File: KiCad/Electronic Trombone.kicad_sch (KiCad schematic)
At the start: 13 parts, among them J1 691137710004, U1 TL074, U3 TL074

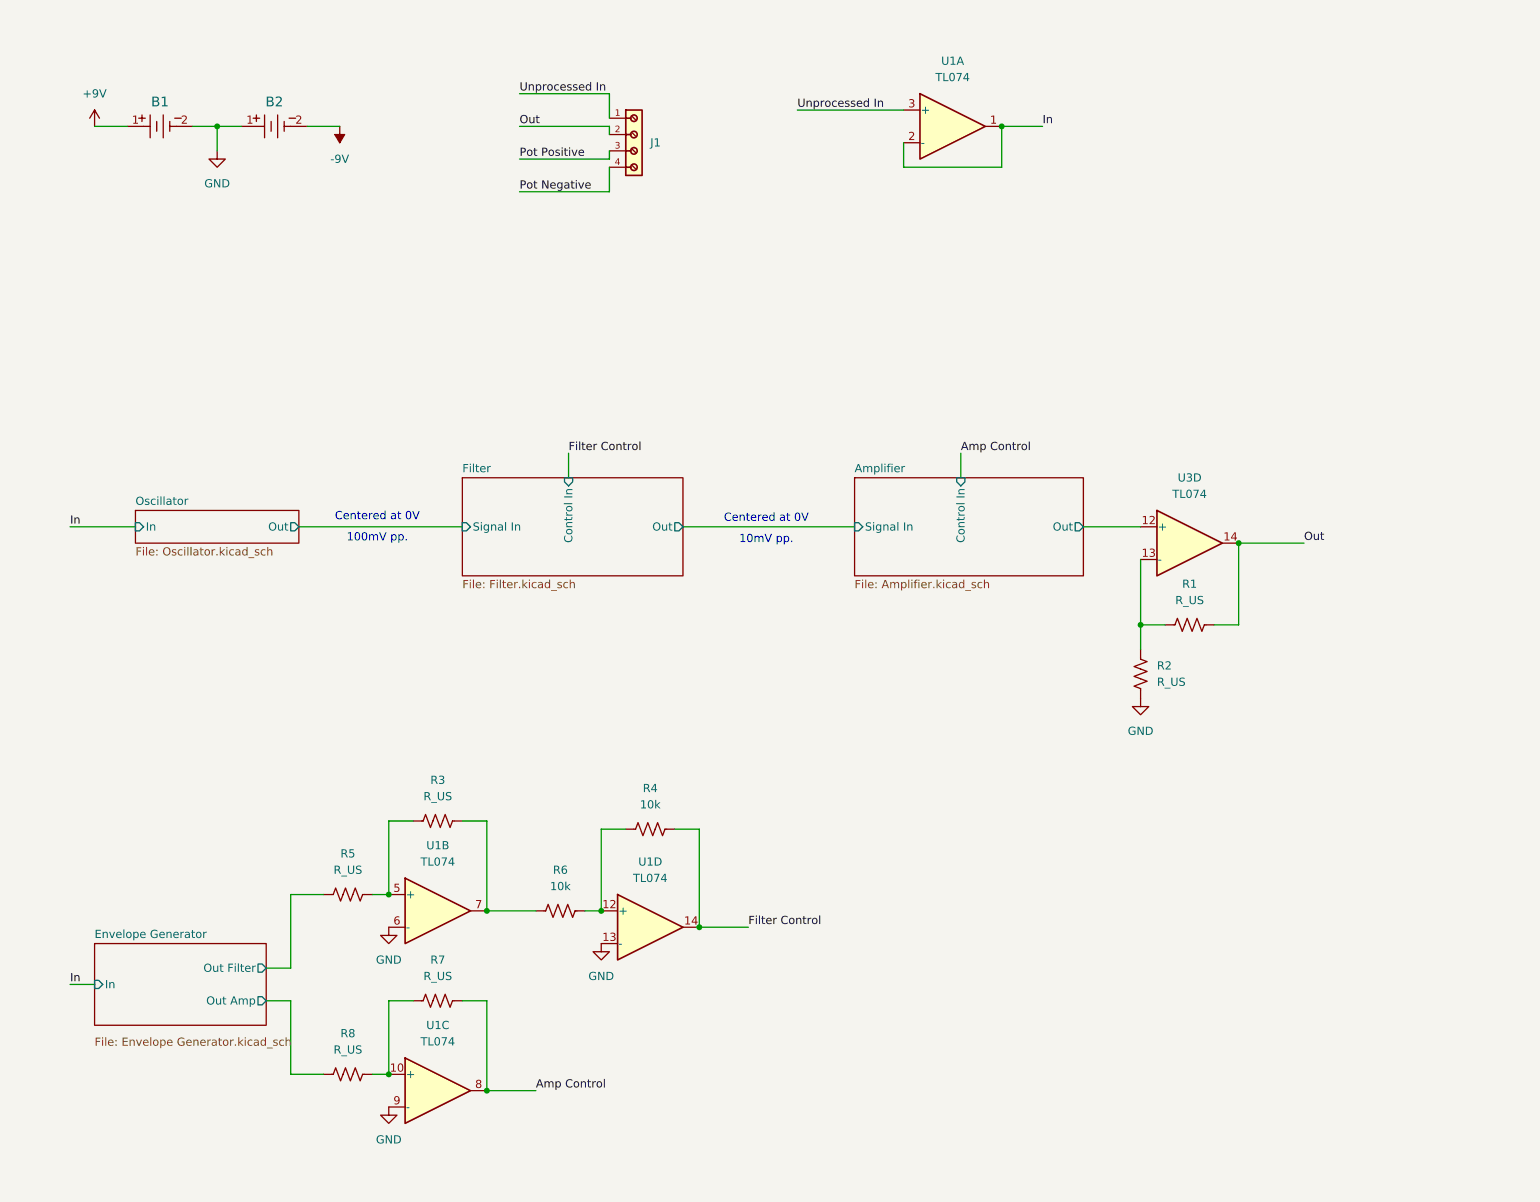
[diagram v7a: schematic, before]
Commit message: updated footprints
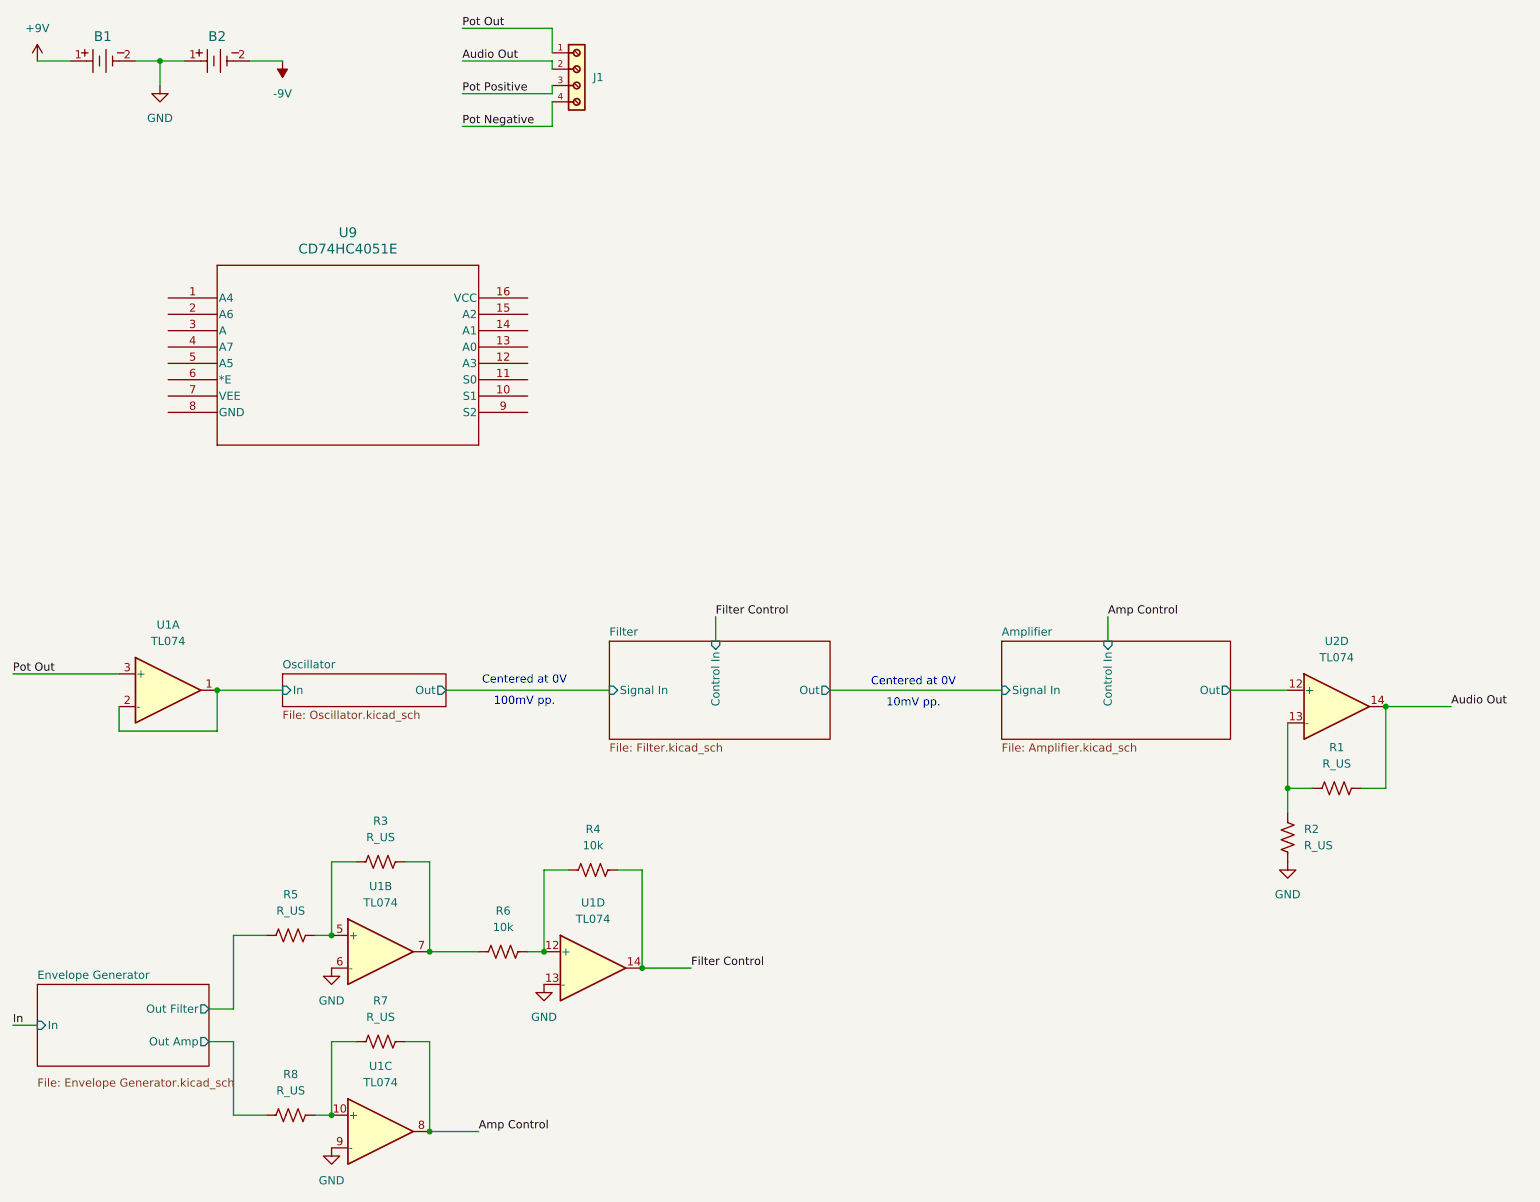
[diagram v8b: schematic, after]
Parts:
- added U9: CD74HC4051E, Mux CD74HC4051E:N16, symbol Mux CD74HC4051E:CD74HC4051E
- J1: footprint 691137710004:691137710004 -> Header 691137710004:691137710004
- R1, R2, R3, R5, R7, R8: footprint (none) -> Resistor_THT:R_Axial_DIN0207_L6.3mm_D2.5mm_P7.62mm_Horizontal
- R4, R6: footprint (none) -> Resistor_SMD:R_0201_0603Metric
- U1: footprint (none) -> Package_DIP:DIP-14_W7.62mm
- U2: renamed from U3; footprint (none) -> Package_DIP:DIP-14_W7.62mm
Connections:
- net In: no longer U1.1, U1.2 (-)
- net Out renamed Audio Out
- net Unprocessed In renamed Pot Out
- new net Oscillator/In: U1.1, U1.2 (-)
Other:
- moved on the sheet: B1, B2, J1, R1, R2, R3, R4, R5, R6, R7, R8, U1B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
